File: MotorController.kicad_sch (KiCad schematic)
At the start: 105 parts, among them IC1 ft234xd, IC2 A3921KLPTR-T, IC3 A3921KLPTR-T, J1 Conn_01x02, J10 Conn_01x02, J11 Conn_02x05_Counter_Clockwise, J2 Conn_01x02, J3 Conn_01x04, J4 Conn_01x04, J5 Conn_01x06, J6 USB_B_Micro, J7 Conn_02x05_Counter_Clockwise, J9 Conn_01x02, Q1 Q_PMOS_GDSD, Q2 GSFQ6806, Q3 GSFQ6806, Q4 GSFQ6806, Q5 GSFQ6806, SW1 SW_SPDT, SW2 SW_Push, U1 STM32F303K8Tx, U2 TPSM13604HNDWR, U4 LXES11D, U5 LMZ12002EXT, Y1 32M

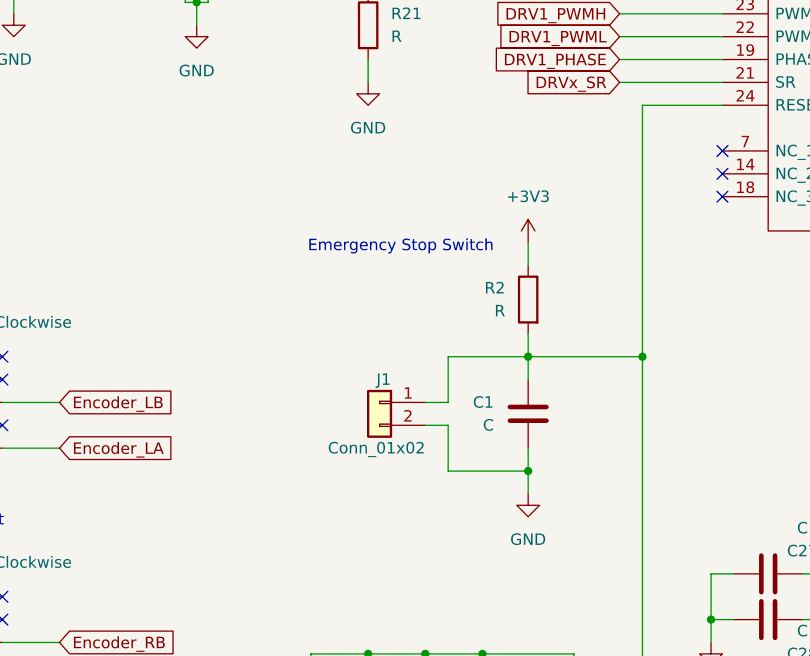
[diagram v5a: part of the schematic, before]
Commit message: 緊急停止スイッチがプッシュオフであることに気が付いてそれを修正
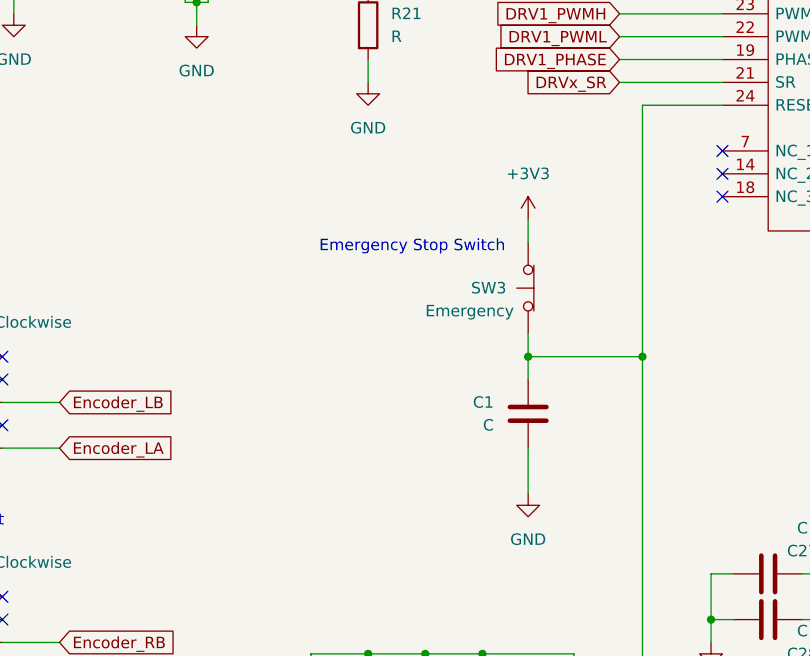
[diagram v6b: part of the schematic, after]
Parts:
- removed J1: Conn_01x02, symbol Connector_Generic:Conn_01x02
- removed R2: R, symbol Device:R
- added SW3: Emergency, symbol Switch:SW_Push_Open
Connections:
- net +3V3: now also SW3.2 (B)
- net at C1.1, IC2.24 (RESET), IC3.24 (RESET): now also SW3.1 (A)
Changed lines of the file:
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@@
   (junction (at 207.01 210.82) (diameter 0) (color 0 0 0 0)
   )
-  (junction (at 245.11 113.03) (diameter 0) (color 0 0 0 0)
-  )
   (junction (at 36.83 193.04) (diameter 0) (color 0 0 0 0)
   )
@@
     (stroke (width 0) (type default))
   )
-  (wire (pts (xy 233.68 107.95) (xy 236.22 107.95))
-    (stroke (width 0) (type default))
-  )
   (wire (pts (xy 285.75 203.2) (xy 285.75 200.66))
     (stroke (width 0) (type default))
@@
     (stroke (width 0) (type default))
   )
-  (wire (pts (xy 236.22 105.41) (xy 233.68 105.41))
-    (stroke (width 0) (type default))
-  )
   (wire (pts (xy 218.44 193.04) (xy 207.01 193.04))
     (stroke (width 0) (type default))
@@
     (stroke (width 0) (type default))
   )
-  (wire (pts (xy 245.11 110.49) (xy 245.11 113.03))
+  (wire (pts (xy 245.11 110.49) (xy 245.11 115.57))
     (stroke (width 0) (type default))
   )
@@
     (stroke (width 0) (type default))
   )
+  (wire (pts (xy 245.11 85.09) (xy 245.11 87.63))
+    (stroke (width 0) (type default))
+  )
   (wire (pts (xy 339.09 185.42) (xy 339.09 186.69))
     (stroke (width 0) (type default))
@@
     (stroke (width 0) (type default))
   )
-  (wire (pts (xy 245.11 113.03) (xy 236.22 113.03))
-    (stroke (width 0) (type default))
-  )
   (wire (pts (xy 161.29 73.66) (xy 161.29 76.2))
     (stroke (width 0) (type default))
@@
     (stroke (width 0) (type default))
   )
-  (wire (pts (xy 245.11 87.63) (xy 245.11 90.17))
-    (stroke (width 0) (type default))
-  )
   (wire (pts (xy 227.33 153.67) (xy 266.7 153.67))
     (stroke (width 0) (type default))
@@
     (stroke (width 0) (type default))
   )
-  (wire (pts (xy 236.22 107.95) (xy 236.22 113.03))
-    (stroke (width 0) (type default))
-  )
   (wire (pts (xy 186.69 137.16) (xy 193.04 137.16))
     (stroke (width 0) (type default))
@@
     (stroke (width 0) (type default))
   )
-  (wire (pts (xy 245.11 113.03) (xy 245.11 115.57))
-    (stroke (width 0) (type default))
-  )
   (wire (pts (xy 99.06 210.82) (xy 101.6 210.82))
     (stroke (width 0) (type default))
@@
     (stroke (width 0) (type default))
   )
-  (wire (pts (xy 245.11 100.33) (xy 236.22 100.33))
-    (stroke (width 0) (type default))
-  )
   (wire (pts (xy 275.59 124.46) (xy 279.4 124.46))
     (stroke (width 0) (type default))
@@
     (stroke (width 0) (type default))
   )
-  (wire (pts (xy 236.22 100.33) (xy 236.22 105.41))
-    (stroke (width 0) (type default))
-  )
   (wire (pts (xy 124.46 48.26) (xy 140.97 48.26))
     (stroke (width 0) (type default))
@@
     (effects (font (size 1.27 1.27)) (justify left bottom))
   )
-  (text "Emergency Stop Switch" (at 241.3 88.9 0)
+  (text "Emergency Stop Switch" (at 242.57 88.9 0)
     (effects (font (size 1.27 1.27)) (justify right bottom))
   )
@@
     )
   )
-  (symbol (lib_id "Connector_Generic:Conn_01x02") (at 228.6 105.41 0) (mirror y) (unit 1)
-    (in_bom yes) (on_board yes) (dnp no)
-    (property "Reference" "J1" (at 229.87 102.87 0)
-      (effects (font (size 1.27 1.27)) (justify left))
-    )
-    (property "Value" "Conn_01x02" (at 233.68 110.49 0)
-      (effects (font (size 1.27 1.27)) (justify left))
-    )
-    (property "Footprint" "" (at 228.6 105.41 0)
-      (effects (font (size 1.27 1.27)) hide)
-    )
-    (property "Datasheet" "~" (at 228.6 105.41 0)
-      (effects (font (size 1.27 1.27)) hide)
-    )
-    (pin "1")
-    (pin "2")
-    (instances
-      (project "MotorController"
-        (path "/5f98a318-5528-4c4b-bcf3-90ead89a063c"
-          (reference "J1") (unit 1)
-        )
-      )
-    )
-  )
   (symbol (lib_id "power:GND") (at 111.76 63.5 0) (unit 1)
     (in_bom yes) (on_board yes) (dnp no) (fields_autoplaced)
@@
     )
   )
-  (symbol (lib_id "Device:R") (at 245.11 93.98 0) (mirror y) (unit 1)
-    (in_bom yes) (on_board yes) (dnp no) (fields_autoplaced)
-    (property "Reference" "R2" (at 242.57 92.71 0)
-      (effects (font (size 1.27 1.27)) (justify left))
-    )
-    (property "Value" "R" (at 242.57 95.25 0)
-      (effects (font (size 1.27 1.27)) (justify left))
-    )
-    (property "Footprint" "" (at 246.888 93.98 90)
-      (effects (font (size 1.27 1.27)) hide)
-    )
-    (property "Datasheet" "~" (at 245.11 93.98 0)
-      (effects (font (size 1.27 1.27)) hide)
-    )
-    (pin "1")
-    (pin "2")
-    (instances
-      (project "MotorController"
-        (path "/5f98a318-5528-4c4b-bcf3-90ead89a063c"
-          (reference "R2") (unit 1)
-        )
-      )
-    )
-  )
   (symbol (lib_id "power:+3V3") (at 218.44 187.96 0) (unit 1)
     (in_bom yes) (on_board yes) (dnp no) (fields_autoplaced)
@@
     )
   )
-  (symbol (lib_id "power:+3V3") (at 245.11 87.63 0) (mirror y) (unit 1)
+  (symbol (lib_id "power:+3V3") (at 245.11 85.09 0) (mirror y) (unit 1)
     (in_bom yes) (on_board yes) (dnp no) (fields_autoplaced)
-    (property "Reference" "#PWR07" (at 245.11 91.44 0)
+    (property "Reference" "#PWR07" (at 245.11 88.9 0)
       (effects (font (size 1.27 1.27)) hide)
     )
-    (property "Value" "+3V3" (at 245.11 82.55 0)
+    (property "Value" "+3V3" (at 245.11 80.01 0)
       (effects (font (size 1.27 1.27)))
     )
-    (property "Footprint" "" (at 245.11 87.63 0)
+    (property "Footprint" "" (at 245.11 85.09 0)
       (effects (font (size 1.27 1.27)) hide)
     )
-    (property "Datasheet" "" (at 245.11 87.63 0)
+    (property "Datasheet" "" (at 245.11 85.09 0)
       (effects (font (size 1.27 1.27)) hide)
     )
@@
         )
       )
+    )
+  )
+  (symbol (lib_id "Switch:SW_Push_Open") (at 245.11 92.71 90) (unit 1)
+    (in_bom yes) (on_board yes) (dnp no)
+    (property "Reference" "SW3" (at 238.76 92.71 90)
+      (effects (font (size 1.27 1.27)) (justify right))
+    )
+    (property "Value" "Emergency" (at 233.68 95.25 90)
+      (effects (font (size 1.27 1.27)) (justify right))
+    )
+    (property "Footprint" "" (at 240.03 92.71 0)
+      (effects (font (size 1.27 1.27)) hide)
+    )
+    (property "Datasheet" "~" (at 240.03 92.71 0)
+      (effects (font (size 1.27 1.27)) hide)
+    )
+    (pin "1")
+    (pin "2")
+    (instances
+      (project "MotorController"
+        (path "/5f98a318-5528-4c4b-bcf3-90ead89a063c"
+          (reference "SW3") (unit 1)
+        )
+      )

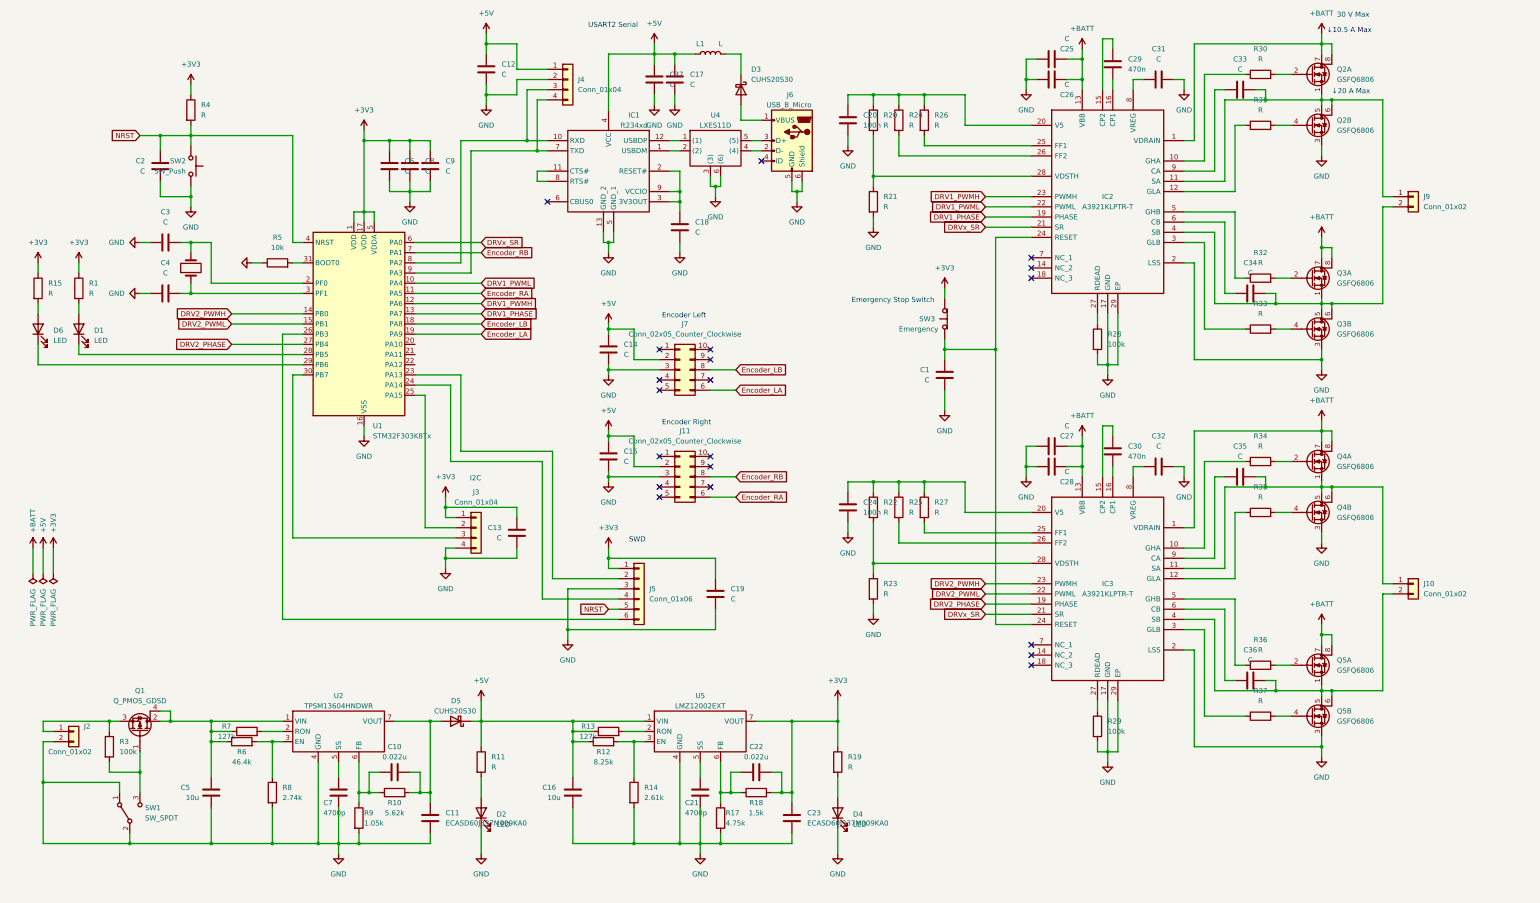
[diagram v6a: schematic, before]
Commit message: コネクタの形状を記しておいた。余ったピンで CAN トランシーバ使えるようにした。ERC 通した。PDF も更新した
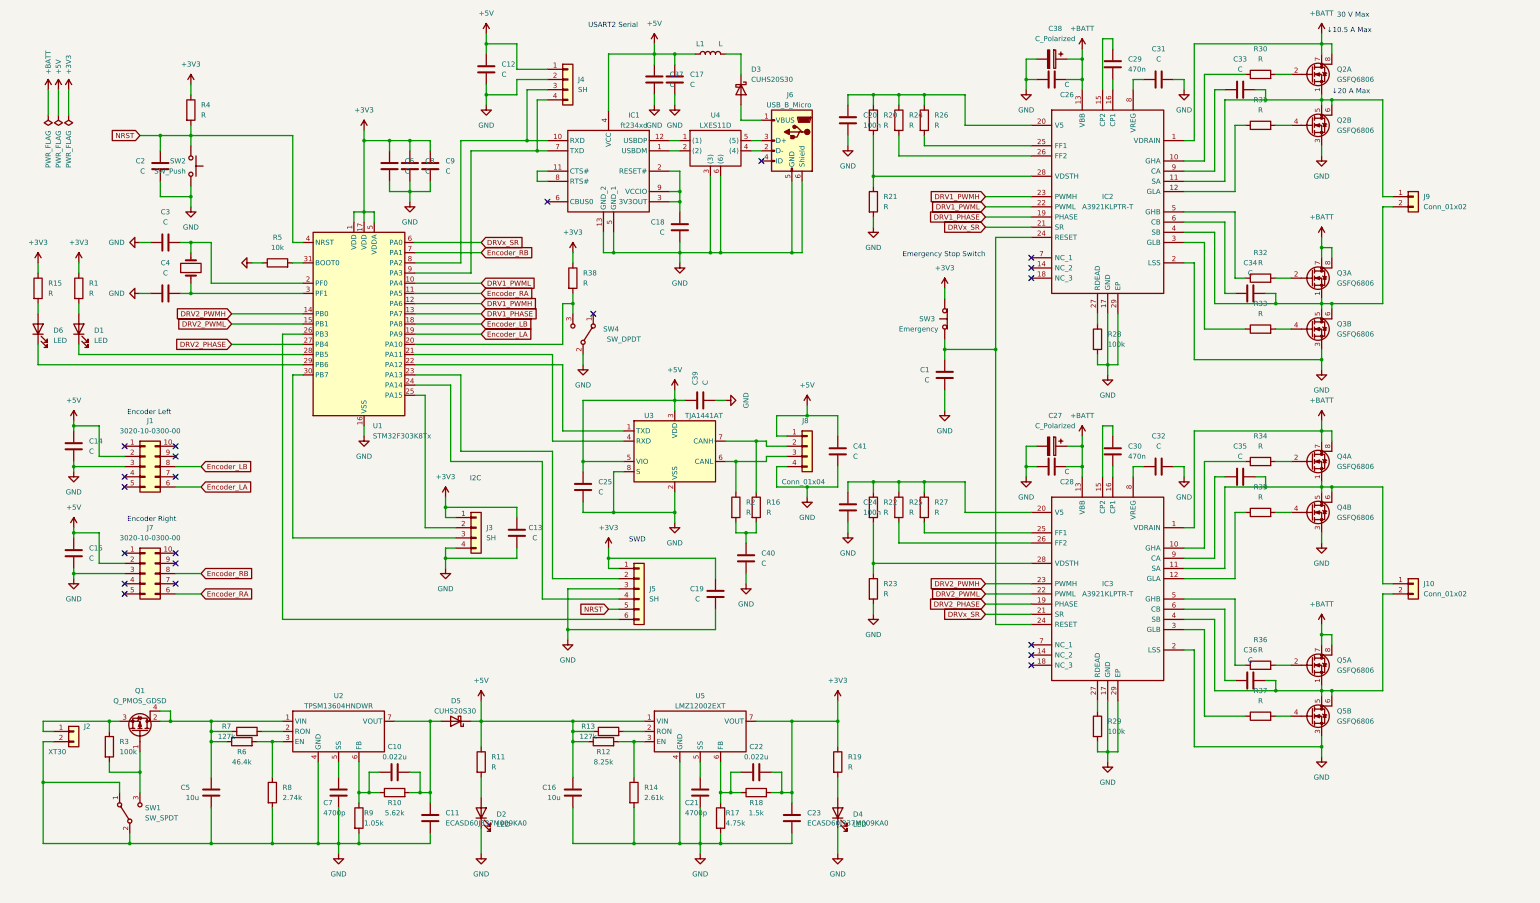
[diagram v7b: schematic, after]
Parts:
- removed C27: C, symbol Device:C
- removed J11: Conn_02x05_Counter_Clockwise, symbol Connector_Generic:Conn_02x05_Counter_Clockwise
- added C27, C38: C_Polarized, symbol Device:C_Polarized
- added C39, C40, C41: C, symbol Device:C
- added J1: 3020-10-0300-00, symbol Connector_Generic:Conn_02x05_Counter_Clockwise
- added J8: Conn_01x04, symbol Connector_Generic:Conn_01x04
- added R16, R2, R38: R, symbol Device:R
- added SW4: SW_DPDT, symbol Switch:SW_SPDT
- added U3: TJA1441AT, Package_SO:SOIC-8_3.9x4.9mm_P1.27mm, symbol Interface_CAN_LIN:MCP2558FD-xSN
- J2: value Conn_01x02 -> XT30
- J3, J4: value Conn_01x04 -> SH
- J5: value Conn_01x06 -> SH
- J7: value Conn_02x05_Counter_Clockwise -> 3020-10-0300-00
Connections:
- net +3V3: now also R38.1
- net +5V: now also C25.1, C39.1, C41.1, J1.2 (Pin_2), J8.1 (Pin_1), U3.3 (VDD), U3.5 (VIO)
- net +BATT: now also C27.1, C38.1; no longer C25.2
- net Encoder_LA: now also J1.6 (Pin_6); no longer J7.6 (Pin_6)
- net Encoder_LB: now also J1.8 (Pin_8); no longer J7.8 (Pin_8)
- net Encoder_RA: now also J7.6 (Pin_6)
- net Encoder_RB: now also J7.8 (Pin_8)
- net GND: now also C25.2, C27.2, C38.2, C39.2, C40.2, C41.2, J1.3 (Pin_3), J8.4 (Pin_4), SW4.2 (B), U3.2 (VSS), U3.8 (S); no longer C25.1
- net at U1.20 (PA10): now also R38.2, SW4.3 (C)
- net at U1.21 (PA11): now also U3.4 (RXD)
- net at U1.22 (PA12): now also U3.1 (TXD)
- new net: J8.2 (Pin_2), R16.1, U3.7 (CANH)
- new net: C40.1, R16.2, R2.2
- new net: J8.3 (Pin_3), R2.1, U3.6 (CANL)
- no-connect marks 20 -> 21

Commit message: power flag の指定方法を変えた。+BATT の位置を Pch FET の前に置いた
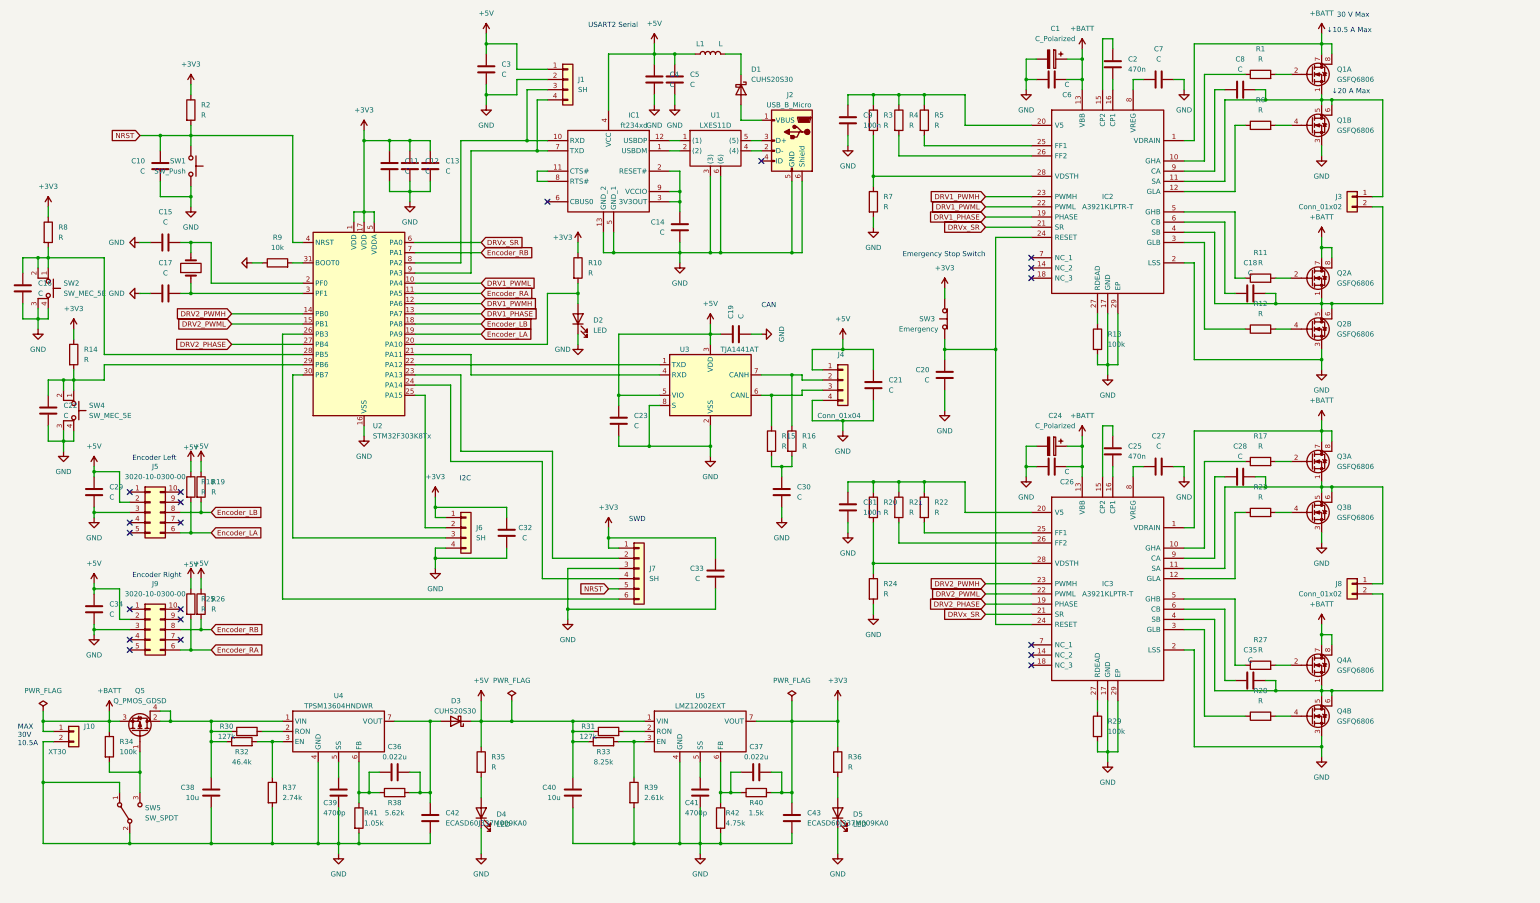
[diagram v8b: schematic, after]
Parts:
- removed C15: C, symbol Device:C
- removed D1, D6: LED, symbol Device:LED
- removed J7: 3020-10-0300-00, symbol Connector_Generic:Conn_02x05_Counter_Clockwise
- removed R15: R, symbol Device:R
- removed SW4: SW_DPDT, symbol Switch:SW_SPDT
- added C16, C22, C34: C, symbol Device:C
- added D2: LED, symbol Device:LED
- added J9: 3020-10-0300-00, symbol Connector_Generic:Conn_02x05_Counter_Clockwise
- added R14, R18, R19, R25, R26: R, symbol Device:R
- added SW2, SW4: SW_MEC_5E, symbol Switch:SW_MEC_5E
- IC1: footprint SON45P300X300X80-13N-D -> LibraryLoader:SON45P300X300X80-13N-D
- IC2, IC3: footprint A3944KLPTRT -> LibraryLoader:A3944KLPTRT
- renumbered C38 to C1, C2 to C10, C6 to C11, C8 to C12, C9 to C13, C18 to C14, C3 to C15, C4 to C17, C34 to C18, C39 to C19, C29 to C2, C1 to C20, C41 to C21, C25 to C23, C27 to C24, C30 to C25, C28 to C26, C32 to C27, C35 to C28, C14 to C29, C12 to C3, C40 to C30, C24 to C31, C13 to C32, C19 to C33, C36 to C35, C10 to C36, C22 to C37, C5 to C38, C7 to C39, C37 to C4, C16 to C40, C21 to C41, C11 to C42, C23 to C43, C17 to C5, C26 to C6, C31 to C7, C33 to C8, C20 to C9, D3 to D1, D5 to D3, D2 to D4, D4 to D5, J4 to J1, J2 to J10, J6 to J2, J9 to J3, J8 to J4, J1 to J5, J3 to J6, J5 to J7, J10 to J8, Q2 to Q1, Q3 to Q2, Q4 to Q3, Q5 to Q4, Q1 to Q5, R30 to R1, R38 to R10, R32 to R11, R33 to R12, R28 to R13, R2 to R15, R34 to R17, R4 to R2, R22 to R20, R25 to R21, R27 to R22, R35 to R23, R23 to R24, R36 to R27, R37 to R28, R20 to R3, R7 to R30, R13 to R31, R6 to R32, R12 to R33, R3 to R34, R11 to R35, R19 to R36, R8 to R37, R10 to R38, R14 to R39, R24 to R4, R18 to R40, R9 to R41, R17 to R42, R26 to R5, R31 to R6, R21 to R7, R1 to R8, R5 to R9, SW2 to SW1, SW1 to SW5, U4 to U1, U1 to U2, U2 to U4
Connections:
- net +3V3: now also R14.1
- net +5V: now also C34.1, J9.2 (Pin_2), R18.1, R19.1, R25.1, R26.1
- net +BATT: now also J10.1 (Pin_1), Q5.3 (S), R34.1
- net Encoder_LA: now also R18.2
- net Encoder_LB: now also R19.2
- net Encoder_RA: now also J9.6 (Pin_6), R25.2
- net Encoder_RB: now also J9.8 (Pin_8), R26.2
- net GND: now also C16.2, C22.2, C34.2, D2.1 (K), J9.3 (Pin_3), SW2.3 (K), SW2.4 (A), SW4.3 (K), SW4.4 (A)
- net at R10.2, U2.20 (PA10): now also D2.2 (A)
- net at U2.28 (PB5): now also R8.2, C16.1, SW2.1, SW2.2
- net at U2.29 (PB6): now also C22.1, R14.2, SW4.1, SW4.2
- no-connect marks 21 -> 20
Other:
- note added: "CAN"
- note added: "MAX 30V 10.5A"
- moved on the sheet: C19, C21, C23, C29, C30, C32, C33, J3, J4, J5, J6, J7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
